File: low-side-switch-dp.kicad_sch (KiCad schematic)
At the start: 4 parts, among them Q24 2N6517BU

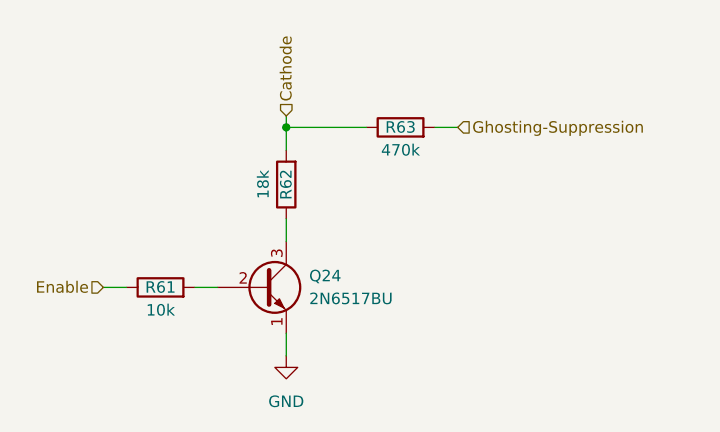
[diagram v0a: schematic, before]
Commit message: Update values to soldered ones
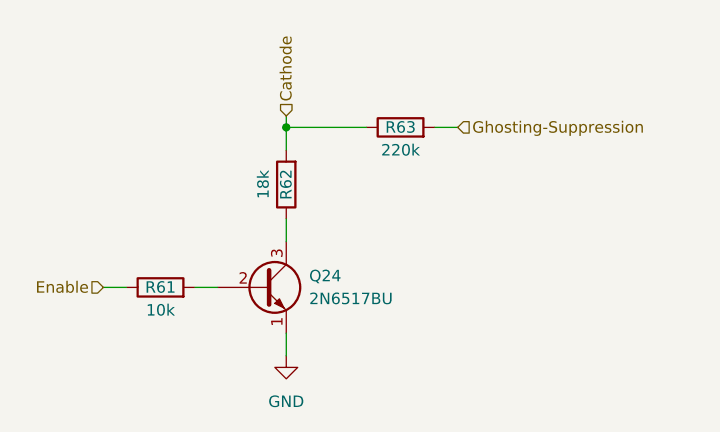
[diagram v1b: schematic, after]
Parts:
- R63: value 470k -> 220k
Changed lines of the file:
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@@
 			)
 		)
-		(property "Value" "470k"
+		(property "Value" "220k"
 			(at 180.34 85.09 90)
 			(effects
